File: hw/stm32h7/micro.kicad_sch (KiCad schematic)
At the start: 30 parts, among them J1 USB_C_Receptacle, J2 TC2030, SW1 MCU Reset, SW2 MCU Reset, U1 USBLC6-2P6, U2 STM32H743VIHx

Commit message: WIP: H7 dual-axis encoder ports, VSENSE, LED swap, TPS2553/ESD on J4
- driver sheet: respaced; DRV8316C 3x-PWM pinout; J4 encoder port with
  100R series, 2.2k/5.1k pull-ups, TPD4E05U06 ESD array, TPS2553 current
  limited 5V switch (ENC_EN/ENC_SW_nFLT); phase VSENSE dividers
  (100k/8.2k, 8.2p/100p compensated); R55/R58/R62 footprint -> R_0201
- root sheet: second driver instance (driver2) for the dual-axis plan
- micro sheet: D1/D2 -> WS2812B-2020-V6 (3.3V logic), 5V0 feed
- power sheet: drop 3V3_VSENSE_AI (VREFINT instead), LMR50410 cleanup
- stm32h7.ioc: TIM1/TIM8 PWM, SPI2/SPI3/SPI4, TIM4 encoder, FDCAN1/2,
  QUADSPI bank 2
- datasheets: WS2812B-2020-V6, SK6805-EC15, TPS2553
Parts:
- removed D1, D2: SK6805, LED_SMD:LED_SK6805_PLCC4_2.4x2.7mm_P1.3mm, symbol LED:SK6805
- added C15, C18: 0.1uF, Capacitor_SMD:C_0201_0603Metric, symbol Device:C_Small
- added D1, D2: WS2812B-2020, pcs_lib:LED_WS2812B-2020_PLCC4_2.0x2.0mm, symbol pcs_bldc_sym_lib:WS2812B-2020
- added R3: 0R, Resistor_SMD:R_0201_0603Metric, symbol Device:R_Small
- added TP3: 5V0_VSENSE, TestPoint:TestPoint_Pad_1.0x1.0mm, symbol Connector:TestPoint_Small
- renumbered C15 to C16, C16 to C17, R3 to R4, R4 to R5
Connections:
- net GND: now also C15.1, C18.1, D1.2 (VSS), D2.2 (VSS)
- net SWCLK: now also U2.A9 (PA14)
- net SWDIO: now also U2.A10 (PA13)
- net SWO: now also U2.A7 (PB3)
- new net: D1.1 (DOUT), D2.3 (DIN)
- new net: D1.3 (DIN), R3.1
- new net: D2.1 (DOUT), TP3.1
- new net 5V0: C15.2, C18.2, D1.4 (VDD), D2.4 (VDD)
- new net RGB_DIN: R3.2
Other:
- note added: "RGB LEDs"
- note removed: "replace with SK6805-EC15"

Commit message: WIP: schematic bringup
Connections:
- net ENC1_A_MISO: now reaches U2.A6 (PB4)
- net ENC1_B_MOSI: now reaches U2.C5 (PB5)
- net ENC1_Z_CS: now reaches U2.E9 (PC9)
- net ENC2_Z_CS: now reaches U2.G8 (PD15)
- net ENC2_A_MISO: now reaches U2.H10 (PB14)
- net ENC2_A_MISO: now also U2.K10 (PD12)
- net ENC1_SCK: now reaches U2.H3 (PA5)
- net ENC2_B_MOSI: now reaches U2.J10 (PD13)

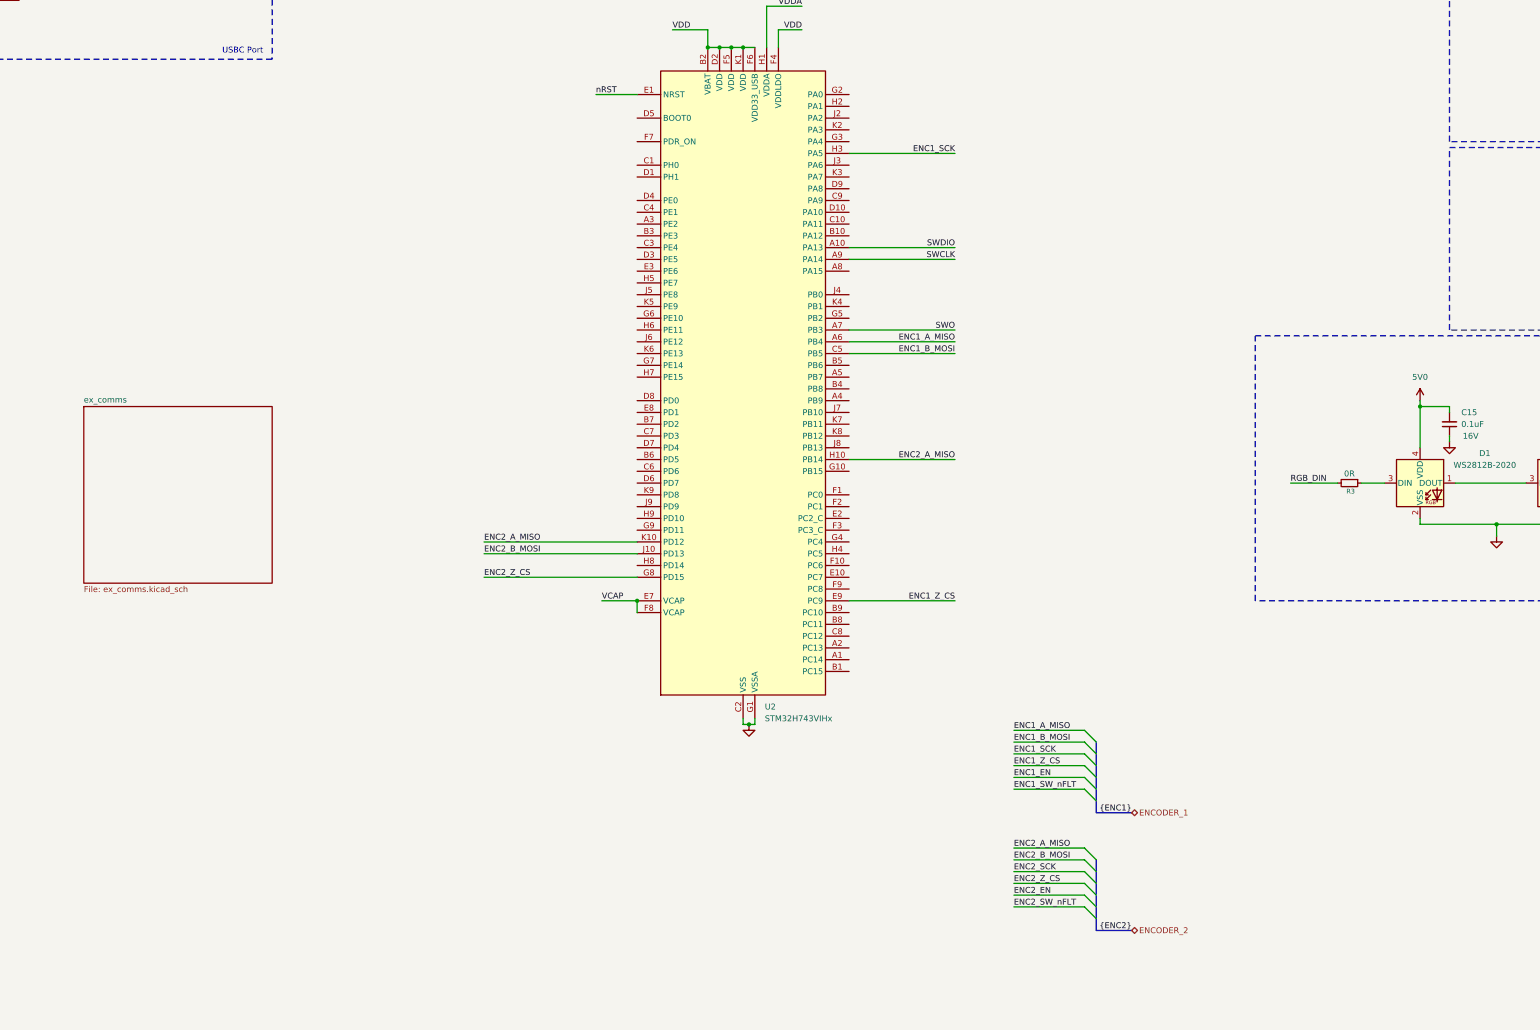
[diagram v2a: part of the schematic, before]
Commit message: WIP: H7 pin plan complete on micro sheet + .ioc, expansion 5V switch
- micro: QSPI bank 2, FDCAN1/2, USB, SPI4 DRV bus + nCS, driver
  nSLEEP/DRVOFF/INLx GPIOs, TIM15_CH1 RGB_DIN, USR_BTN1, LAN9252
  IRQ/SYNC0/SYNC1/nRST, USART3 + RS485 DE, I2C1 to expansion header
- micro: TPS2553 nFAULT wire-OR -> PWR_nFLT (PD11), EXP_PWR_EN on PD0,
  ENC2_SCK moved to PD3
- power: TPS2553 switched 5V0_EXP rail for the expansion header (~1A)
- .ioc: matching assignments, TIM15 and USART3/I2C1 added, PB11 dropped
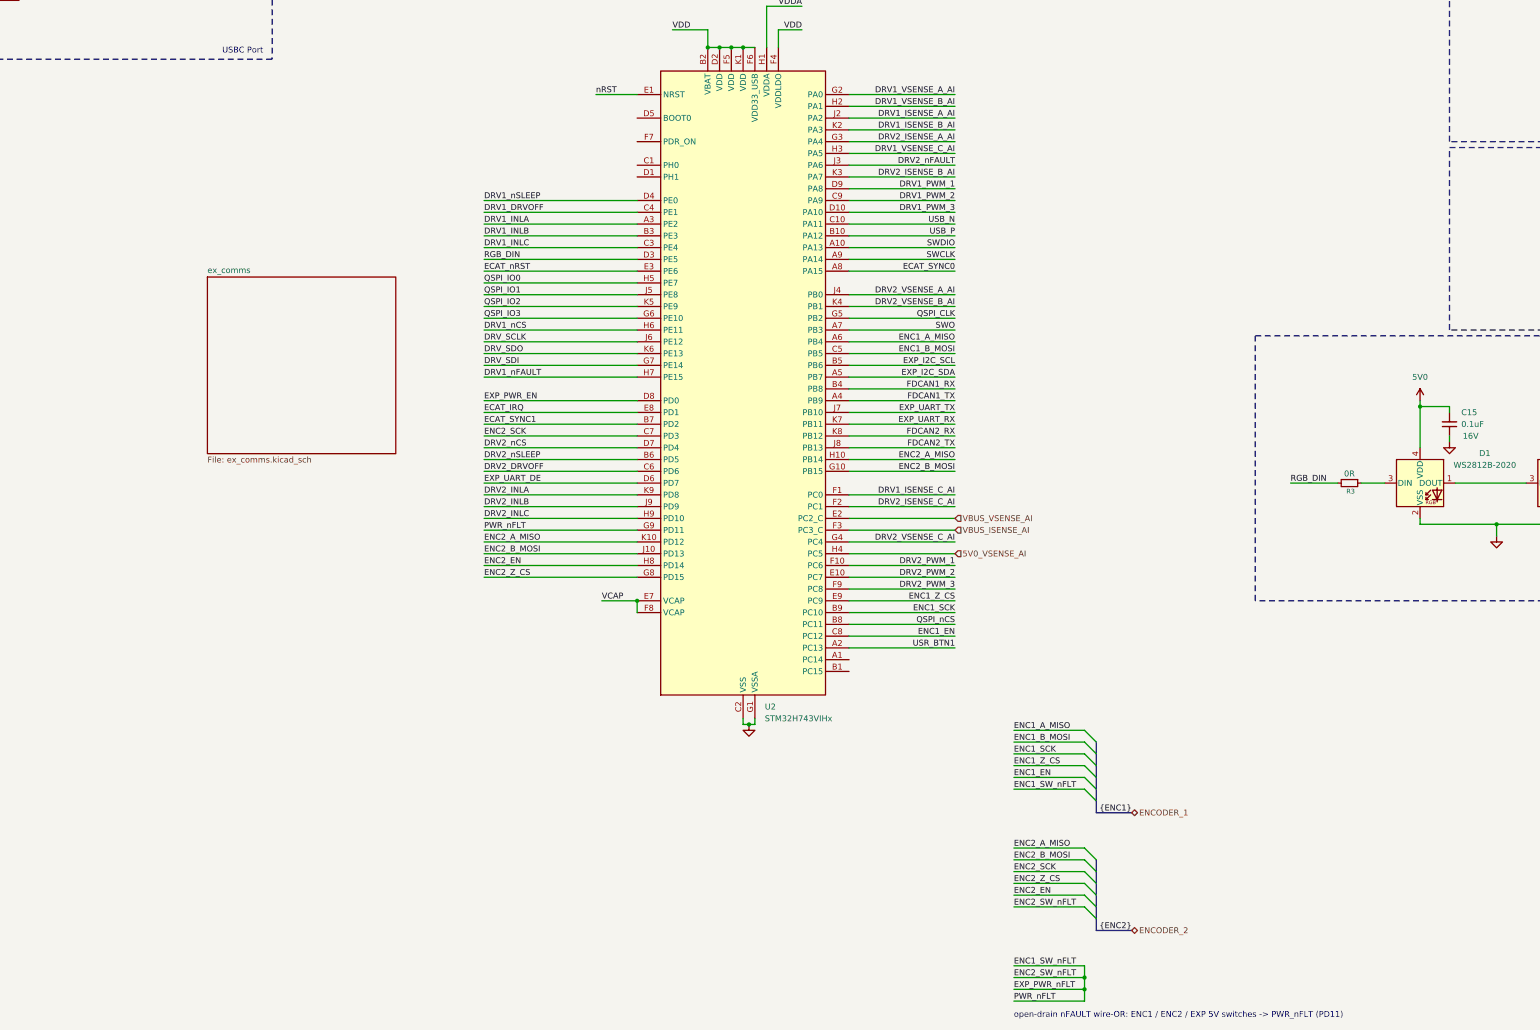
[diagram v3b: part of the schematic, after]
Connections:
- net ENC1_EN: now also U2.C8 (PC12)
- net ENC1_SCK: now also U2.B9 (PC10); no longer U2.H3 (PA5)
- net ENC1_SW_nFLT: now also U2.G9 (PD11)
- net ENC2_B_MOSI: now also U2.G10 (PB15)
- net ENC2_EN: now also U2.H8 (PD14)
- net ENC2_SCK: now also U2.C7 (PD3)
- net RGB_DIN: now also U2.D3 (PE5)
- net USB_N: now also U2.C10 (PA11)
- net USB_P: now also U2.B10 (PA12)
- net USR_BTN1: now also U2.A2 (PC13)
- net DRV1_INLA: now reaches U2.A3 (PE2)
- net FDCAN1_TX: now reaches U2.A4 (PB9)
- net EXP_I2C_SDA: now reaches U2.A5 (PB7)
- net ECAT_SYNC0: now reaches U2.A8 (PA15)
- net DRV1_INLB: now reaches U2.B3 (PE3)
- net FDCAN1_RX: now reaches U2.B4 (PB8)
- net EXP_I2C_SCL: now reaches U2.B5 (PB6)
- net DRV2_nSLEEP: now reaches U2.B6 (PD5)
- net ECAT_SYNC1: now reaches U2.B7 (PD2)
- net QSPI_nCS: now reaches U2.B8 (PC11)
- net DRV1_INLC: now reaches U2.C3 (PE4)
- net DRV1_DRVOFF: now reaches U2.C4 (PE1)
- net DRV2_DRVOFF: now reaches U2.C6 (PD6)
- net DRV1_PWM_2: now reaches U2.C9 (PA9)
- net DRV1_PWM_3: now reaches U2.D10 (PA10)
- net DRV1_nSLEEP: now reaches U2.D4 (PE0)
- net EXP_UART_DE: now reaches U2.D6 (PD7)
- net DRV2_nCS: now reaches U2.D7 (PD4)
- net EXP_PWR_EN: now reaches U2.D8 (PD0)
- net DRV1_PWM_1: now reaches U2.D9 (PA8)
- net DRV2_PWM_2: now reaches U2.E10 (PC7)
- net VBUS_VSENSE_AI: now reaches U2.E2 (PC2_C)
- net ECAT_nRST: now reaches U2.E3 (PE6)
- net ECAT_IRQ: now reaches U2.E8 (PD1)
- net DRV1_ISENSE_C_AI: now reaches U2.F1 (PC0)
- net DRV2_PWM_1: now reaches U2.F10 (PC6)
- net DRV2_ISENSE_C_AI: now reaches U2.F2 (PC1)
- net VBUS_ISENSE_AI: now reaches U2.F3 (PC3_C)
- net DRV2_PWM_3: now reaches U2.F9 (PC8)
- net DRV1_VSENSE_A_AI: now reaches U2.G2 (PA0)
- net DRV2_ISENSE_A_AI: now reaches U2.G3 (PA4)
- net DRV2_VSENSE_C_AI: now reaches U2.G4 (PC4)
- net QSPI_CLK: now reaches U2.G5 (PB2)
- net QSPI_IO3: now reaches U2.G6 (PE10)
- net DRV_SDI: now reaches U2.G7 (PE14)
- net DRV1_VSENSE_B_AI: now reaches U2.H2 (PA1)
- net 5V0_VSENSE_AI: now reaches U2.H4 (PC5)
- net QSPI_IO0: now reaches U2.H5 (PE7)
- net DRV1_nCS: now reaches U2.H6 (PE11)
- net DRV1_nFAULT: now reaches U2.H7 (PE15)
- net DRV2_INLC: now reaches U2.H9 (PD10)
- net DRV1_ISENSE_A_AI: now reaches U2.J2 (PA2)
- net DRV2_nFAULT: now reaches U2.J3 (PA6)
- net DRV2_VSENSE_A_AI: now reaches U2.J4 (PB0)
- net QSPI_IO1: now reaches U2.J5 (PE8)
- net DRV_SCLK: now reaches U2.J6 (PE12)
- net EXP_UART_TX: now reaches U2.J7 (PB10)
- net FDCAN2_TX: now reaches U2.J8 (PB13)
- net DRV2_INLB: now reaches U2.J9 (PD9)
- net DRV1_ISENSE_B_AI: now reaches U2.K2 (PA3)
- net DRV2_ISENSE_B_AI: now reaches U2.K3 (PA7)
- net DRV2_VSENSE_B_AI: now reaches U2.K4 (PB1)
- net QSPI_IO2: now reaches U2.K5 (PE9)
- net DRV_SDO: now reaches U2.K6 (PE13)
- net EXP_UART_RX: now reaches U2.K7 (PB11)
- net FDCAN2_RX: now reaches U2.K8 (PB12)
- net DRV2_INLA: now reaches U2.K9 (PD8)
- new net DRV1_VSENSE_C_AI: U2.H3 (PA5)
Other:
- note added: "open-drain nFAULT wire-OR: ENC1 / ENC2 / EXP 5V switches -> PWR_nFLT (PD11)"

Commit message: WIP: H7 schematic and PCB layout progress
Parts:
- removed TP2: 5V0_VSENSE, TestPoint:TestPoint_Pad_1.0x1.0mm, symbol Connector:TestPoint_Small
- added C19, C20, C23, C24: 0.1uF, Capacitor_SMD:C_0201_0603Metric, symbol Device:C_Small
- added C3, C5: 8pF, Capacitor_SMD:C_0201_0603Metric, symbol Device:C_Small
- added D2, D4, D5, D6: WS2812B-2020, pcs_lib:LED_WS2812B-2020_PLCC4_2.0x2.0mm, symbol pcs_bldc_sym_lib:WS2812B-2020
- added R3: 5.1k, Resistor_SMD:R_0201_0603Metric, symbol Device:R_Small
- added R4, R8: 0R, Resistor_SMD:R_0201_0603Metric, symbol Device:R_Small
- added Y1: 25MHz, Crystal:Crystal_SMD_SeikoEpson_FA128-4Pin_2.0x1.6mm, symbol !TIMING:ECS-240-12-37B-CKY-TR
- SW2: value MCU Reset -> USR_BTN1
- TP1: renamed from TP3; value 5V0_VSENSE -> EXT_RGB_DIN
- TP2: renamed from TP1; value 5V0_VSENSE -> nRST
- renumbered C8 to C10, C9 to C11, C10 to C12, C11 to C13, C12 to C14, C13 to C15, C14 to C16, C15 to C17, C16 to C21, C17 to C22, C3 to C4, C4 to C6, C5 to C7, C6 to C8, C7 to C9, D2 to D3, J1 to J6, J2 to J7, R3 to R5, R4 to R6, R5 to R7
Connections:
- net 3V3: now also R3.1
- net 5V0: now also C19.2, C20.2, C23.2, C24.2, D2.4 (VDD), D4.4 (VDD), D5.4 (VDD), D6.4 (VDD)
- net DRV_SDO: now also R3.2
- net GND: now also C19.1, C20.1, C23.1, C24.1, C3.1, C5.1, D2.2 (VSS), D4.2 (VSS), D5.2 (VSS), D6.2 (VSS), Y1.2 (GND), Y1.4 (GND)
- net at D3.1 (DOUT): now also D5.3 (DIN); no longer TP1.1
- net RCC_OSC_IN: now reaches U2.C1 (PH0)
- net RCC_OSC_IN: now also C3.2, Y1.3 (X2)
- net RCC_OSC_OUT: now reaches U2.D1 (PH1)
- net RCC_OSC_OUT: now also R4.1
- new net: D6.1 (DOUT), R8.2
- new net: D2.1 (DOUT), D4.3 (DIN)
- new net: D2.3 (DIN), D5.1 (DOUT)
- new net: C5.2, R4.2, Y1.1 (X1)
- new net: D4.1 (DOUT), D6.3 (DIN)
- new net EXT_RGB_DIN: R8.1, TP1.1
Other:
- sheet ex_comms ports: added ECAT_IRQ, ECAT_SYNC0, ECAT_SYNC1, ECAT_nRST, EXP_5V0, EXP_I2C_SCL, EXP_I2C_SDA, EXP_UART_DE, EXP_UART_RX, EXP_UART_TX, FDCAN1_RX, FDCAN1_TX, FDCAN2_RX, FDCAN2_TX, QSPI_CLK, QSPI_IO0, QSPI_IO1, QSPI_IO2, QSPI_IO3, QSPI_nCS, RGB_DIN; removed none
- note added: "What to do about BOOT0? add a switch?"
- note removed: "open-drain nFAULT wire-OR: ENC1 / ENC2 / EXP 5V switches -> PWR_nFLT (PD11)"
- moved on the sheet: C17, D1, D3, R5, TP1
